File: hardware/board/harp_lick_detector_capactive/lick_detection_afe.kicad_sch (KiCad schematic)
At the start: 74 parts, among them J3 Conn_Triaxial, U10 AD8652, U13 ADS7049, U14 MAX4564EKA, U6 ADA4891-4, U7 LTC6268xS8-10, U8 REF2025, U9 TS5A9411DCKR

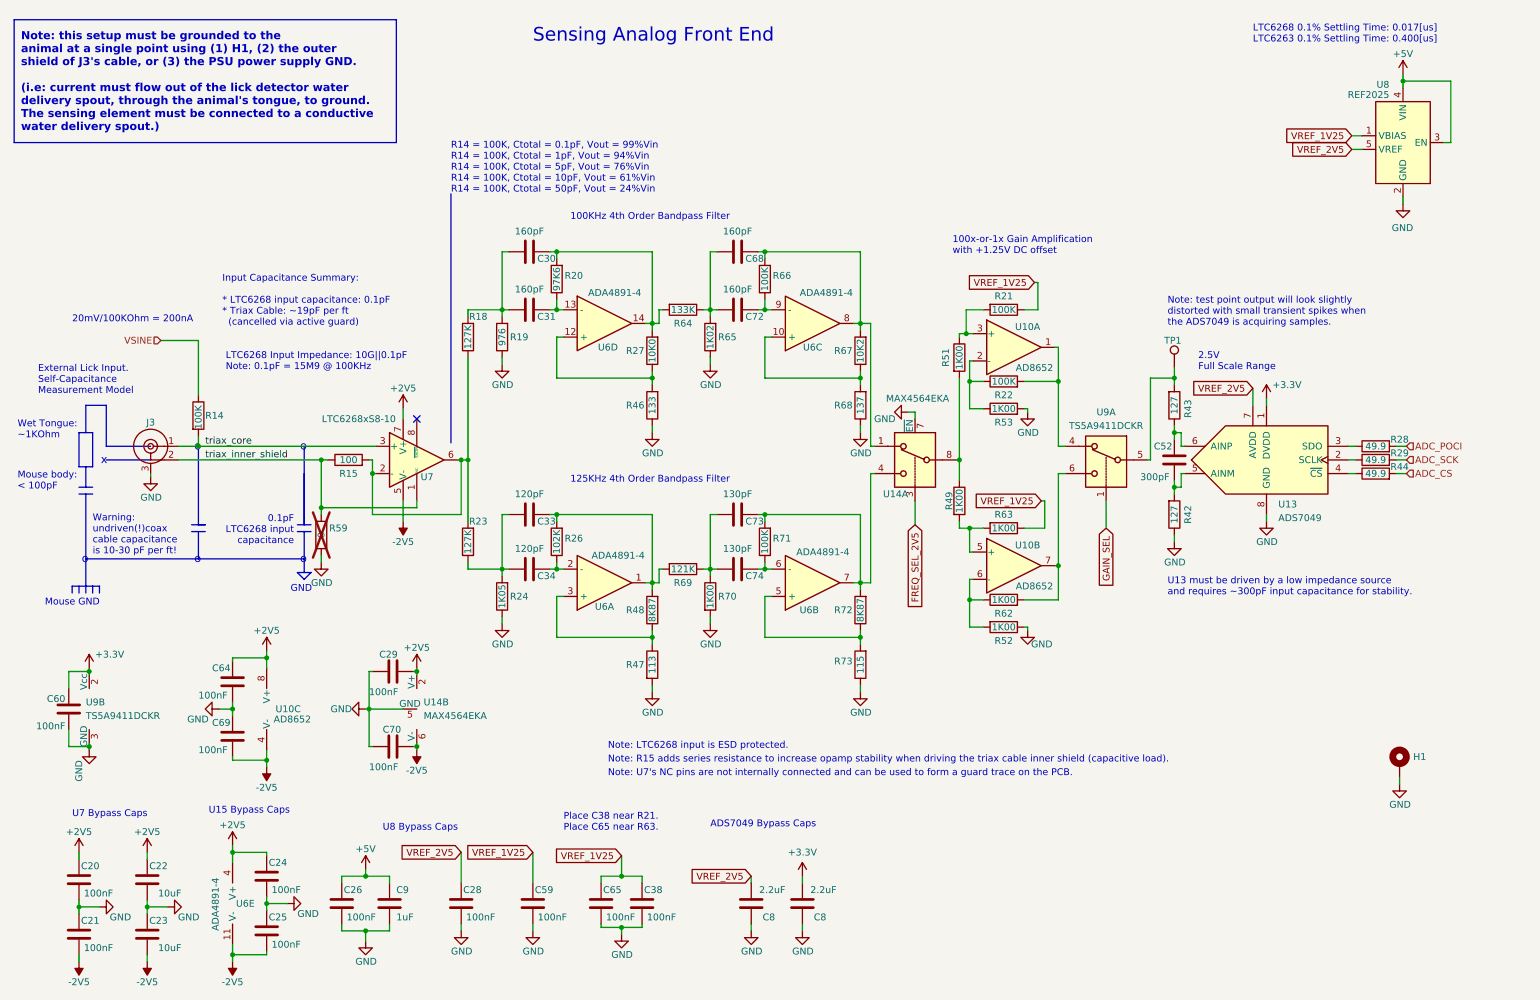
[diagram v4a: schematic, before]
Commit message: v0.8 pcb draft ready; schematic components up to date
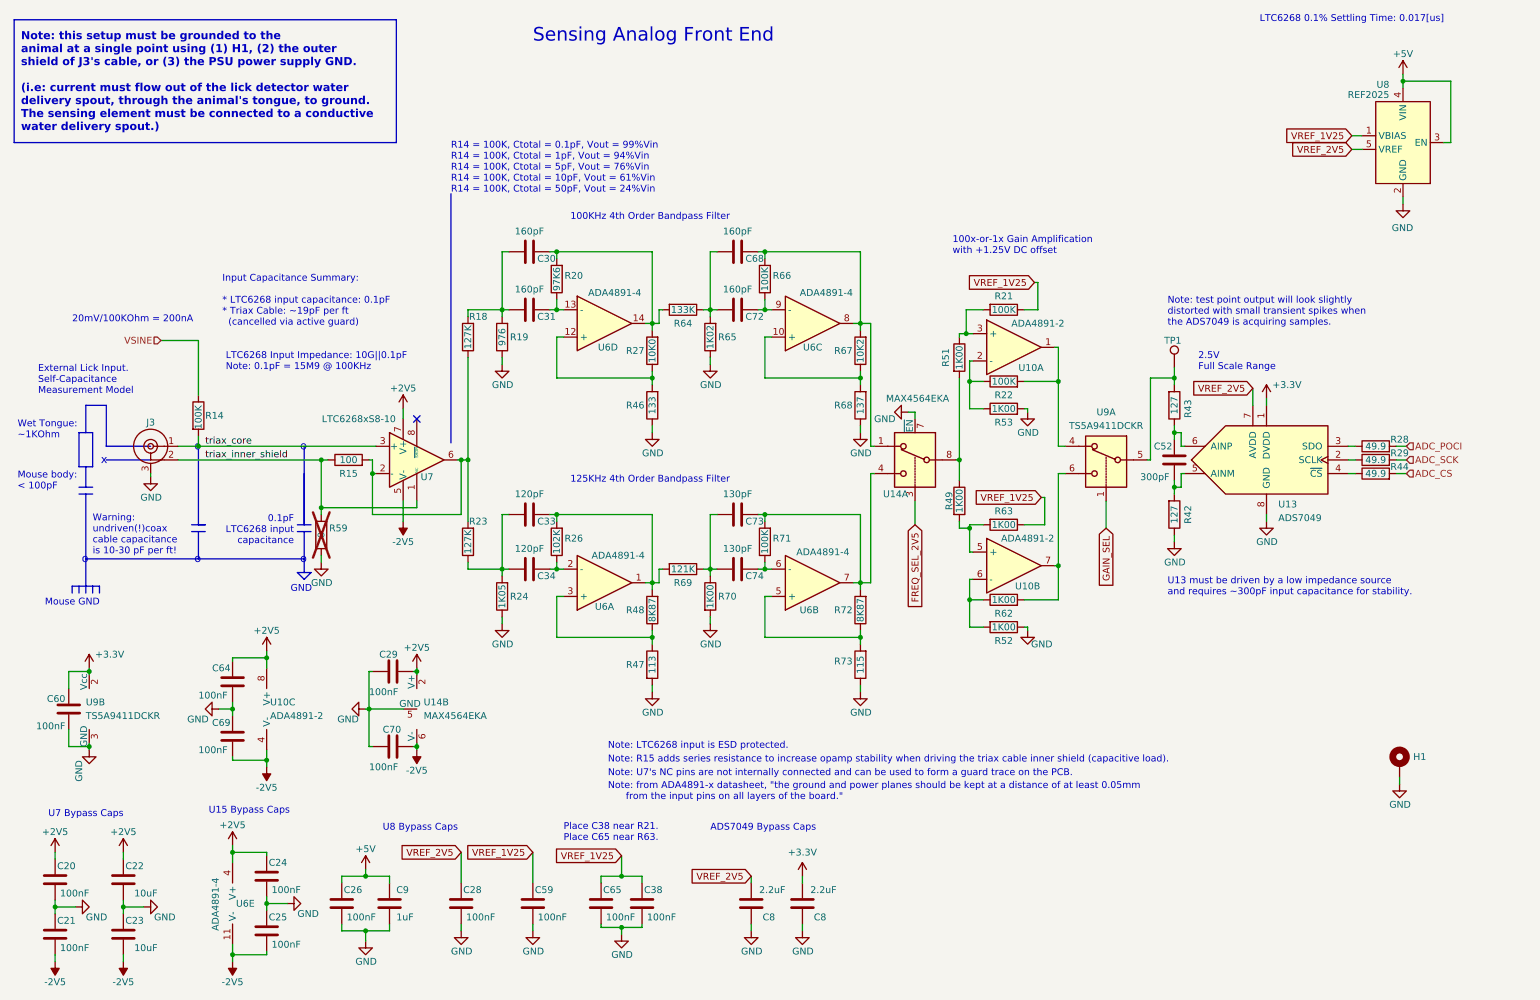
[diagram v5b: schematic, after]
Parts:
- removed U10: AD8652, Package_SO:MSOP-8_3x3mm_P0.65mm, symbol kicad_component_library:AD8652
- added U10: ADA4891-2, Package_SO:MSOP-8_3x3mm_P0.65mm, symbol kicad_component_library:ADA4891-2
- U6: Link (none) -> https://www.digikey.com/en/products/detail/analog-devices-i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; Manufacturer (none) -> Analog Devices Inc.; Manufacturer Number (none) -> ADA4891-4WARUZ-R7; Notes (none) -> Recommended bypass capacitor size is 0508.
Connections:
- net +2V5: now also U10.8 (V+)
- net -2V5: now also U10.4 (V-)
- net at R21.2, R51.1: now also U10.3 (+)
- net at R22.1, R53.1: now also U10.2 (-)
- net at R22.2, U9.4: now also U10.1
- net at R52.2, R62.1: now also U10.6 (-)
- net at R62.2, U9.6: now also U10.7
- net at R49.2, R63.2: now also U10.5 (+)
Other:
- note added: "LTC6268 0.1% Settling Time: 0.017[us]"
- note added: "Note: from ADA4891-x datasheet, "the ground and power planes should be kept at a distance of at least 0.05mm from the input pins on all layers of the board.""
- note removed: "LTC6268 0.1% Settling Time: 0.017[us] LTC6263 0.1% Settling Time: 0.400[us]"
- moved on the sheet: C20, C21, C22, C23, R63

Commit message: finish rev8
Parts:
- R59: Alternate (none) -> n/a; Link (none) -> n/a; Manufacturer (none) -> n/a; Manufacturer Number (none) -> n/a
- TP1: Alternate (none) -> n/a; Link (none) -> n/a
- U14: Link (none) -> https://www.digikey.com/en/products/detail/analog-devices-i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; Manufacturer (none) -> Analog Devices Inc./Maxim Integrated; Manufacturer Number (none) -> MAX4564EKA+T
- U9: Link (none) -> https://www.digikey.com/en/products/detail/texas-instrument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; Manufacturer (none) -> Texas Instruments; Manufacturer Number (none) -> TS5A9411DCKR
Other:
- note added: "100x"
- note added: "1x"
- moved on the sheet: C30, C31, C33, C34, C52, C68, C72, C73, C74, R19, R20, R21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

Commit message: update to new harp core
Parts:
- added C66, C75: 100nF, Capacitor_SMD:C_0402_1005Metric, symbol Device:C
- added U15: MAX4564EKA, Package_TO_SOT_SMD:SOT-23-8, symbol kicad_component_library:MAX4564EKA+T
- R21, R22: value 100K -> 62K; Link https://www.digikey.com/en/products/detail/yageo/RT0402BRD07100KL/1068989 -> https://www.digikey.com/en/products/detail/yageo/RT0402BRD0762KL/1069354; Manufacturer Number RT0402BRD07100KL -> RT0402BRD0762KL
- renumbered C9 to C27, C8 to C50, C8 to C51
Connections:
- net +2V5: now also C66.1, U15.2 (V+)
- net -2V5: now also C75.1, U15.6 (V-)
- net GND: now also C66.2, C75.2, U15.5 (GND), U15.7 (~{EN})
- new net: R51.2, U15.1
- new net: R49.1, U15.4
- new net: U14.8, U15.8
- new net GAIN_SEL_2V5: U15.3
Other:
- note added: "62x"
- note added: "62x-or-1x Gain Amplification with +1.25V DC offset"
- note added: "Second SPDT switch (U15A) prevents switch resistance from interacting with would-be-jointed 1x and 100x amplifiers."
- note removed: "100x"
- note removed: "100x-or-1x Gain Amplification with +1.25V DC offset"
- moved on the sheet: C29, C30, C31, C33, C34, C60, C64, C68, C69, C70, C72, C73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
